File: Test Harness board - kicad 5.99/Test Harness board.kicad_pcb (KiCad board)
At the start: 4 copper layers, 233 x 70 mm, 32 parts, among them U1 TCA9548APWR

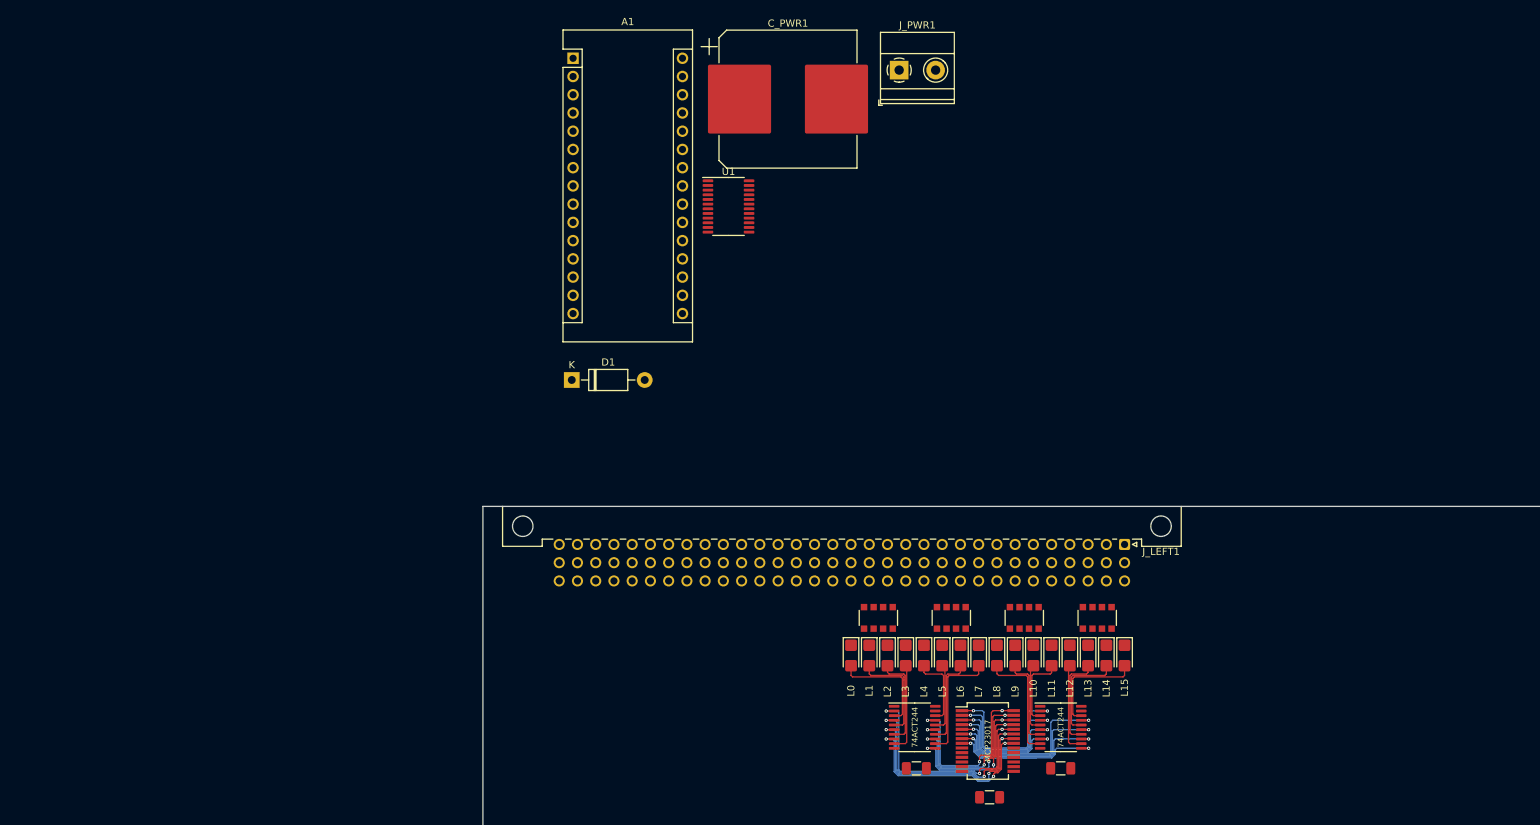
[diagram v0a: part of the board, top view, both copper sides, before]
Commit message: add the components to display the MAR bits
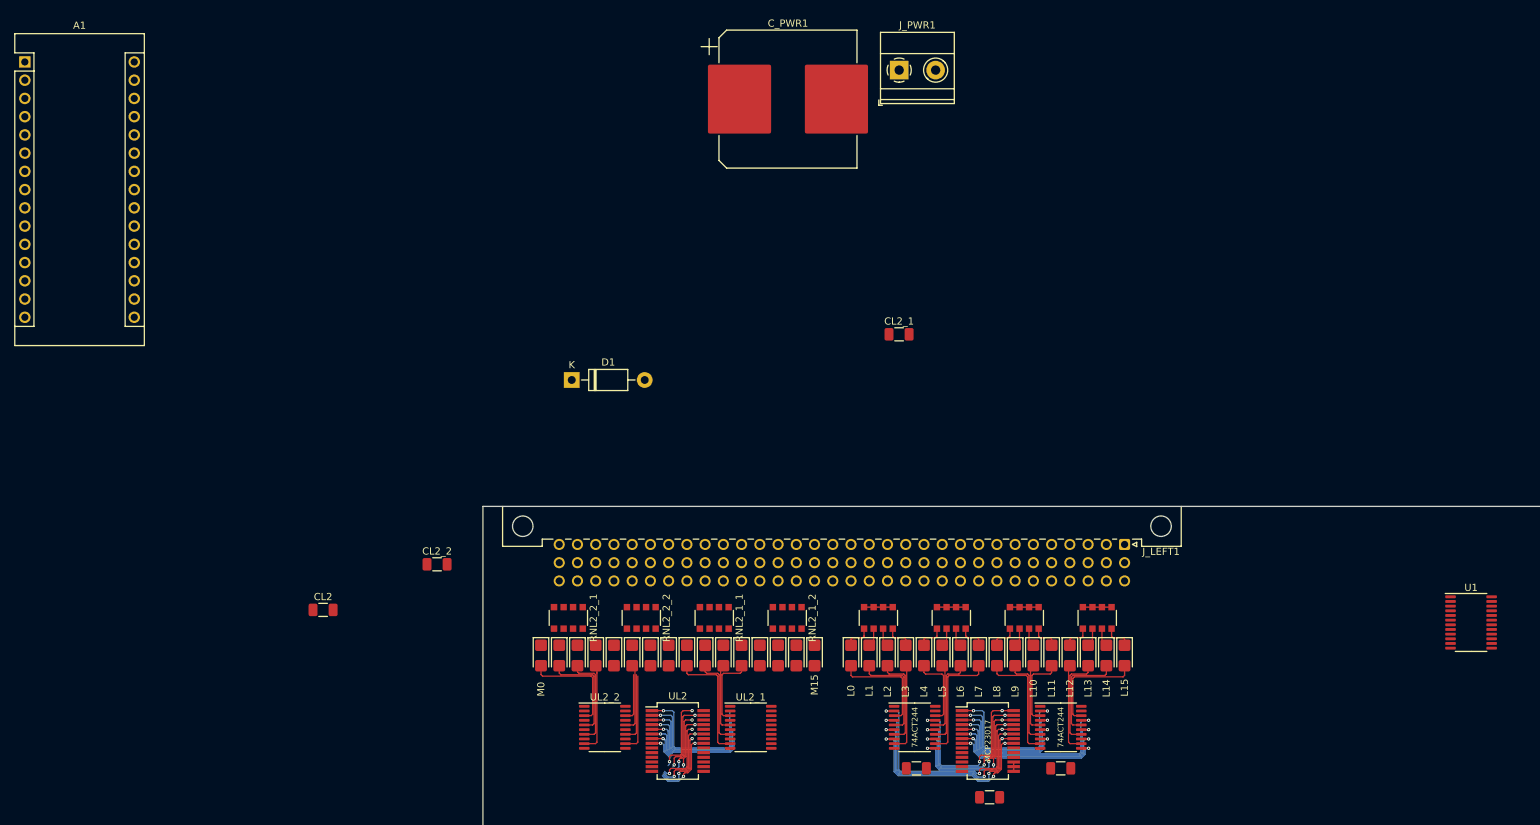
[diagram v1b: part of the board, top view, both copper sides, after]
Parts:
- added CL2: C_Small, Capacitor_SMD:C_1206_3216Metric, F.Cu at (9.74, 84.4)
- added CL2_1: C_Small, Capacitor_SMD:C_1206_3216Metric, F.Cu at (90.0, 46.0)
- added CL2_2: C_Small, Capacitor_SMD:C_1206_3216Metric, F.Cu at (25.6, 78.1)
- added D_MAR0: LED_Small, LED_SMD:LED_1206_3216Metric_Castellated, F.Cu at (40.1, 90.8)
- added D_MAR1: LED_Small, LED_SMD:LED_1206_3216Metric_Castellated, F.Cu at (42.6, 90.8)
- added D_MAR10: LED_Small, LED_SMD:LED_1206_3216Metric_Castellated, F.Cu at (65.5, 90.8)
- added D_MAR11: LED_Small, LED_SMD:LED_1206_3216Metric_Castellated, F.Cu at (68.0, 90.8)
- added D_MAR12: LED_Small, LED_SMD:LED_1206_3216Metric_Castellated, F.Cu at (70.6, 90.8)
- added D_MAR13: LED_Small, LED_SMD:LED_1206_3216Metric_Castellated, F.Cu at (73.1, 90.8)
- added D_MAR14: LED_Small, LED_SMD:LED_1206_3216Metric_Castellated, F.Cu at (75.7, 90.8)
- added D_MAR15: LED_Small, LED_SMD:LED_1206_3216Metric_Castellated, F.Cu at (78.2, 90.8)
- added D_MAR2: LED_Small, LED_SMD:LED_1206_3216Metric_Castellated, F.Cu at (45.2, 90.8)
- added D_MAR3: LED_Small, LED_SMD:LED_1206_3216Metric_Castellated, F.Cu at (47.7, 90.8)
- added D_MAR4: LED_Small, LED_SMD:LED_1206_3216Metric_Castellated, F.Cu at (50.2, 90.8)
- added D_MAR5: LED_Small, LED_SMD:LED_1206_3216Metric_Castellated, F.Cu at (52.8, 90.8)
- added D_MAR6: LED_Small, LED_SMD:LED_1206_3216Metric_Castellated, F.Cu at (55.3, 90.8)
- added D_MAR7: LED_Small, LED_SMD:LED_1206_3216Metric_Castellated, F.Cu at (57.9, 90.8)
- added D_MAR8: LED_Small, LED_SMD:LED_1206_3216Metric_Castellated, F.Cu at (60.4, 90.8)
- added D_MAR9: LED_Small, LED_SMD:LED_1206_3216Metric_Castellated, F.Cu at (63.0, 90.8)
- added RNL2_1_1: R_Pack04, Resistor_SMD:R_Array_Convex_4x1206, F.Cu at (64.2, 85.5)
- added RNL2_1_2: R_Pack04, Resistor_SMD:R_Array_Convex_4x1206, F.Cu at (74.4, 85.5)
- added RNL2_2_1: R_Pack04, Resistor_SMD:R_Array_Convex_4x1206, F.Cu at (43.9, 85.5)
- added RNL2_2_2: R_Pack04, Resistor_SMD:R_Array_Convex_4x1206, F.Cu at (54.1, 85.5)
- added UL2: MCP23017, Package_SO:SSOP-28_5.3x10.2mm_P0.65mm, F.Cu at (59.1, 102.7)
- added UL2_1: 74ACT244, Package_SO:TSSOP-20_4.4x6.5mm_P0.65mm, F.Cu at (69.3, 100.8)
- added UL2_2: 74ACT244, Package_SO:TSSOP-20_4.4x6.5mm_P0.65mm, F.Cu at (49.0, 100.8)
- moved U1 118.5 mm to (169.6, 86.2)
- moved A1 76.4 mm to (-31.8, 8.10)
- renumbered C1 to CL1, C1_1 to CL1_1, C1_2 to CL1_2, RN1_1_1 to RNL1_1_1, RN1_1_2 to RNL1_1_2, RN1_2_1 to RNL1_2_1, RN1_2_2 to RNL1_2_2
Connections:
- J_LEFT1 pad a22: Net-(J_LEFT1-Pada22) -> /Left connector/MAR0
- J_LEFT1 pad a23: Net-(J_LEFT1-Pada23) -> /Left connector/MAR1
- J_LEFT1 pad a24: Net-(J_LEFT1-Pada24) -> /Left connector/MAR2
- J_LEFT1 pad a25: Net-(J_LEFT1-Pada25) -> /Left connector/MAR3
- J_LEFT1 pad a26: Net-(J_LEFT1-Pada26) -> /Left connector/MAR4
- J_LEFT1 pad a27: Net-(J_LEFT1-Pada27) -> /Left connector/MAR5
- J_LEFT1 pad a28: Net-(J_LEFT1-Pada28) -> /Left connector/MAR6
- J_LEFT1 pad a29: Net-(J_LEFT1-Pada29) -> /Left connector/MAR7
- J_LEFT1 pad a30: Net-(J_LEFT1-Pada30) -> /Left connector/MAR8
- J_LEFT1 pad a31: Net-(J_LEFT1-Pada31) -> /Left connector/MAR9
- J_LEFT1 pad b1: (no net) -> Net-(J_LEFT1-Padb1)
- J_LEFT1 pad b10: (no net) -> Net-(J_LEFT1-Padb10)
- J_LEFT1 pad b11: (no net) -> Net-(J_LEFT1-Padb11)
- J_LEFT1 pad b12: (no net) -> Net-(J_LEFT1-Padb12)
- J_LEFT1 pad b13: (no net) -> Net-(J_LEFT1-Padb13)
- J_LEFT1 pad b14: (no net) -> Net-(J_LEFT1-Padb14)
- J_LEFT1 pad b15: (no net) -> Net-(J_LEFT1-Padb15)
- J_LEFT1 pad b16: (no net) -> Net-(J_LEFT1-Padb16)
- J_LEFT1 pad b17: (no net) -> Net-(J_LEFT1-Padb17)
- J_LEFT1 pad b18: (no net) -> Net-(J_LEFT1-Padb18)
- J_LEFT1 pad b19: (no net) -> Net-(J_LEFT1-Padb19)
- J_LEFT1 pad b2: (no net) -> Net-(J_LEFT1-Padb2)
- J_LEFT1 pad b20: (no net) -> Net-(J_LEFT1-Padb20)
- J_LEFT1 pad b21: (no net) -> Net-(J_LEFT1-Padb21)
- J_LEFT1 pad b22: (no net) -> Net-(J_LEFT1-Padb22)
- J_LEFT1 pad b23: (no net) -> Net-(J_LEFT1-Padb23)
- J_LEFT1 pad b24: (no net) -> Net-(J_LEFT1-Padb24)
- J_LEFT1 pad b25: (no net) -> Net-(J_LEFT1-Padb25)
- J_LEFT1 pad b26: (no net) -> Net-(J_LEFT1-Padb26)
- J_LEFT1 pad b27: (no net) -> Net-(J_LEFT1-Padb27)
- J_LEFT1 pad b28: (no net) -> Net-(J_LEFT1-Padb28)
- J_LEFT1 pad b29: (no net) -> Net-(J_LEFT1-Padb29)
- J_LEFT1 pad b3: (no net) -> /Left connector/MAR10
- J_LEFT1 pad b30: (no net) -> Net-(J_LEFT1-Padb30)
- J_LEFT1 pad b31: (no net) -> Net-(J_LEFT1-Padb31)
- J_LEFT1 pad b32: (no net) -> Net-(J_LEFT1-Padb32)
- J_LEFT1 pad b4: (no net) -> /Left connector/MAR11
- J_LEFT1 pad b5: (no net) -> /Left connector/MAR12
- J_LEFT1 pad b6: (no net) -> Net-(J_LEFT1-Padb6)
- J_LEFT1 pad b7: (no net) -> /Left connector/MAR13
- J_LEFT1 pad b8: (no net) -> /Left connector/MAR14
- J_LEFT1 pad b9: (no net) -> /Left connector/MAR15
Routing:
- net /Left connector/MAR15: track 0.00 -> 20.6 mm, vias 0 -> 1
- net /Left connector/MAR14: track 0.00 -> 19.2 mm, vias 0 -> 1
- net /Left connector/MAR13: track 0.00 -> 17.7 mm, vias 0 -> 1
- net GND: track 0.00 -> 17.3 mm
- net /Left connector/D_MAR8: track 0.00 -> 16.5 mm
- net /Left connector/MAR12: track 0.00 -> 16.2 mm, vias 0 -> 1
- net /Left connector/D_MAR0: track 0.00 -> 14.9 mm
- net /Left connector/D_MAR1: track 0.00 -> 14.1 mm
- net /Left connector/D_MAR2: track 0.00 -> 13.3 mm
- net /Left connector/D_MAR9: track 0.00 -> 12.7 mm
- net /Left connector/D_MAR3: track 0.00 -> 12.6 mm
- net /Left connector/D_MAR7: track 0.00 -> 11.0 mm
- net /Left connector/MAR0: track 0.00 -> 10.6 mm, vias 0 -> 2
- net /Left connector/D_MAR11: track 0.00 -> 10.5 mm
- net /Left connector/L5: track 31.6 -> 41.7 mm, vias 3 -> 5
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
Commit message: restart on the test harness, made a more compact design (will need the 4 layers though)
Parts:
- added CL3: C_Small, Capacitor_SMD:C_1206_3216Metric, F.Cu at (183.3, 145.9)
- added CL3_1: C_Small, Capacitor_SMD:C_1206_3216Metric, F.Cu at (183.9, 165.8)
- added CL3_2: C_Small, Capacitor_SMD:C_1206_3216Metric, F.Cu at (193.7, 167.4)
- added CL4: C_Small, Capacitor_SMD:C_1206_3216Metric, F.Cu at (191.3, 152.6)
- added CL4_1: C_Small, Capacitor_SMD:C_1206_3216Metric, F.Cu at (191.2, 159.2)
- added CL4_2: C_Small, Capacitor_SMD:C_1206_3216Metric, F.Cu at (64.3, 142.6)
- added CL5: C_Small, Capacitor_SMD:C_1206_3216Metric, F.Cu at (73.4, 140.9)
- added CL5_1: C_Small, Capacitor_SMD:C_1206_3216Metric, F.Cu at (64.9, 144.3)
- added CL5_2: C_Small, Capacitor_SMD:C_1206_3216Metric, F.Cu at (58.0, 142.8)
- added D_A0: LED_Small, LED_SMD:LED_1206_3216Metric_Castellated, F.Cu at (66.7, 106.8)
- added D_A1: LED_Small, LED_SMD:LED_1206_3216Metric_Castellated, F.Cu at (69.2, 106.8)
- added D_A10: LED_Small, LED_SMD:LED_1206_3216Metric_Castellated, F.Cu at (93.9, 106.8)
- added D_A11: LED_Small, LED_SMD:LED_1206_3216Metric_Castellated, F.Cu at (96.4, 106.8)
- added D_A12: LED_Small, LED_SMD:LED_1206_3216Metric_Castellated, F.Cu at (98.9, 106.8)
- added D_A13: LED_Small, LED_SMD:LED_1206_3216Metric_Castellated, F.Cu at (101.4, 106.8)
- added D_A14: LED_Small, LED_SMD:LED_1206_3216Metric_Castellated, F.Cu at (104.7, 106.8)
- added D_A15: LED_Small, LED_SMD:LED_1206_3216Metric_Castellated, F.Cu at (107.2, 106.8)
- added D_A16: LED_Small, LED_SMD:LED_1206_3216Metric_Castellated, F.Cu at (109.7, 106.8)
- added D_A17: LED_Small, LED_SMD:LED_1206_3216Metric_Castellated, F.Cu at (112.2, 106.8)
- added D_A18: LED_Small, LED_SMD:LED_1206_3216Metric_Castellated, F.Cu at (115.4, 106.8)
- added D_A19: LED_Small, LED_SMD:LED_1206_3216Metric_Castellated, F.Cu at (117.9, 106.8)
- added D_A2: LED_Small, LED_SMD:LED_1206_3216Metric_Castellated, F.Cu at (72.4, 106.8)
- added D_A20: LED_Small, LED_SMD:LED_1206_3216Metric_Castellated, F.Cu at (120.4, 106.8)
- added D_A21: LED_Small, LED_SMD:LED_1206_3216Metric_Castellated, F.Cu at (122.9, 106.8)
- added D_A3: LED_Small, LED_SMD:LED_1206_3216Metric_Castellated, F.Cu at (74.9, 106.8)
- added D_A4: LED_Small, LED_SMD:LED_1206_3216Metric_Castellated, F.Cu at (77.4, 106.8)
- added D_A5: LED_Small, LED_SMD:LED_1206_3216Metric_Castellated, F.Cu at (79.9, 106.8)
- added D_A6: LED_Small, LED_SMD:LED_1206_3216Metric_Castellated, F.Cu at (83.2, 106.8)
- added D_A7: LED_Small, LED_SMD:LED_1206_3216Metric_Castellated, F.Cu at (85.7, 106.8)
- added D_A8: LED_Small, LED_SMD:LED_1206_3216Metric_Castellated, F.Cu at (88.2, 106.8)
- added D_A9: LED_Small, LED_SMD:LED_1206_3216Metric_Castellated, F.Cu at (90.7, 106.8)
- added D_D0: LED_Small, LED_SMD:LED_1206_3216Metric_Castellated, F.Cu at (38.4, 106.8)
- added D_D1: LED_Small, LED_SMD:LED_1206_3216Metric_Castellated, F.Cu at (40.9, 106.8)
- added D_D2: LED_Small, LED_SMD:LED_1206_3216Metric_Castellated, F.Cu at (43.4, 106.8)
- added D_D3: LED_Small, LED_SMD:LED_1206_3216Metric_Castellated, F.Cu at (45.9, 106.8)
- added D_D4: LED_Small, LED_SMD:LED_1206_3216Metric_Castellated, F.Cu at (49.2, 106.8)
- added D_D5: LED_Small, LED_SMD:LED_1206_3216Metric_Castellated, F.Cu at (51.7, 106.8)
- added D_D6: LED_Small, LED_SMD:LED_1206_3216Metric_Castellated, F.Cu at (54.2, 106.8)
- added D_D7: LED_Small, LED_SMD:LED_1206_3216Metric_Castellated, F.Cu at (56.7, 106.8)
- added D_IR2: LED_Small, LED_SMD:LED_1206_3216Metric_Castellated, F.Cu at (40.9, 121.8)
- added D_IR3: LED_Small, LED_SMD:LED_1206_3216Metric_Castellated, F.Cu at (43.4, 121.8)
- added D_MEMORY1: LED_Small, LED_SMD:LED_1206_3216Metric_Castellated, F.Cu at (63.9, 121.8)
- added D_MEMREF1: LED_Small, LED_SMD:LED_1206_3216Metric_Castellated, F.Cu at (61.4, 121.8)
- added D_TEST1: LED_Small, LED_SMD:LED_1206_3216Metric_Castellated, F.Cu at (179.6, 151.4)
- added D_TEST2: LED_Small, LED_SMD:LED_1206_3216Metric_Castellated, F.Cu at (202.1, 145.1)
- added D_XL_MDR_HI1: LED_Small, LED_SMD:LED_1206_3216Metric_Castellated, F.Cu at (46.7, 121.8)
- added D_XL_MDR_LO1: LED_Small, LED_SMD:LED_1206_3216Metric_Castellated, F.Cu at (49.2, 121.8)
- added D__IR1: LED_Small, LED_SMD:LED_1206_3216Metric_Castellated, F.Cu at (38.4, 121.8)
- added D__IRQ4: LED_Small, LED_SMD:LED_1206_3216Metric_Castellated, F.Cu at (77.9, 121.8)
- added D__PSEL1: LED_Small, LED_SMD:LED_1206_3216Metric_Castellated, F.Cu at (58.2, 121.8)
- added D__RD1: LED_Small, LED_SMD:LED_1206_3216Metric_Castellated, F.Cu at (54.9, 121.8)
- added D__RESET1: LED_Small, LED_SMD:LED_1206_3216Metric_Castellated, F.Cu at (67.2, 121.8)
- added D__STOP_CLK1: LED_Small, LED_SMD:LED_1206_3216Metric_Castellated, F.Cu at (69.7, 121.8)
- added D__WR1: LED_Small, LED_SMD:LED_1206_3216Metric_Castellated, F.Cu at (52.4, 121.8)
- added RNL3_1_1: R_Pack04, Resistor_SMD:R_Array_Convex_4x1206, F.Cu at (106.4, 101.5)
- added RNL3_1_2: R_Pack04, Resistor_SMD:R_Array_Convex_4x1206, F.Cu at (121.4, 101.5)
- added RNL3_2_1: R_Pack04, Resistor_SMD:R_Array_Convex_4x1206, F.Cu at (85.2, 101.5)
- added RNL3_2_2: R_Pack04, Resistor_SMD:R_Array_Convex_4x1206, F.Cu at (99.7, 101.5)
- added RNL4_1_1: R_Pack04, Resistor_SMD:R_Array_Convex_4x1206, F.Cu at (63.2, 101.5)
- added RNL4_1_2: R_Pack04, Resistor_SMD:R_Array_Convex_4x1206, F.Cu at (78.2, 101.5)
- added RNL4_2_1: R_Pack04, Resistor_SMD:R_Array_Convex_4x1206, F.Cu at (40.2, 101.6)
- added RNL4_2_2: R_Pack04, Resistor_SMD:R_Array_Convex_4x1206, F.Cu at (54.9, 101.6)
- added RNL5_1_1: R_Pack04, Resistor_SMD:R_Array_Convex_4x1206, F.Cu at (63.2, 116.6)
- added RNL5_1_2: R_Pack04, Resistor_SMD:R_Array_Convex_4x1206, F.Cu at (78.7, 116.6)
- added RNL5_2_1: R_Pack04, Resistor_SMD:R_Array_Convex_4x1206, F.Cu at (56.4, 116.6)
- added RNL5_2_2: R_Pack04, Resistor_SMD:R_Array_Convex_4x1206, F.Cu at (40.2, 116.6)
- added UL3: MCP23017, Package_SO:SSOP-28_5.3x10.2mm_P0.65mm, F.Cu at (107.9, 132.3)
- added UL3_1: 74ACT244, Package_SO:TSSOP-20_4.4x6.5mm_P0.65mm, F.Cu at (115.6, 116.7)
- added UL3_2: 74ACT244, Package_SO:TSSOP-20_4.4x6.5mm_P0.65mm, F.Cu at (105.9, 116.7)
- added UL4: MCP23017, Package_SO:SSOP-28_5.3x10.2mm_P0.65mm, F.Cu at (95.3, 118.8)
- added UL4_1: 74ACT244, Package_SO:TSSOP-20_4.4x6.5mm_P0.65mm, F.Cu at (71.1, 115.2)
- added UL4_2: 74ACT244, Package_SO:TSSOP-20_4.4x6.5mm_P0.65mm, F.Cu at (48.2, 115.3)
- added UL5: MCP23017, Package_SO:SSOP-28_5.3x10.2mm_P0.65mm, F.Cu at (95.4, 132.3)
- added UL5_1: 74ACT244, Package_SO:TSSOP-20_4.4x6.5mm_P0.65mm, F.Cu at (54.2, 133.8)
- added UL5_2: 74ACT244, Package_SO:TSSOP-20_4.4x6.5mm_P0.65mm, F.Cu at (40.9, 133.8)
- C_PWR1: footprint Capacitor_SMD:CP_Elec_18x22 -> Capacitor_SMD:CP_Elec_8x10
- D1: value 1N4001 -> 1N4007FLTR; footprint Diode_THT:D_DO-41_SOD81_P10.16mm_Horizontal -> Diode_SMD:D_SOD-123F
- moved A1 194.6 mm to (140.9, 97.8)
- moved J_PWR1 131.5 mm to (129.0, 134.8)
- moved C_PWR1 117.7 mm to (132.2, 115.8)
- moved D1 111.7 mm to (129.0, 125.3), turned to -90 degrees
- moved CL1 94.8 mm to (197.3, 115.0)
- moved CL1_1 94.8 mm to (207.2, 111.0)
- moved CL1_2 94.8 mm to (187.1, 111.0)
- moved UL2 73.1 mm to (132.2, 103.8)
- moved U1 37.2 mm to (148.5, 116.8)
- moved UL1 32.3 mm to (132.2, 90.3)
- moved D_MAR3 2.06 mm to (45.9, 91.8)
- moved D_L12 2.05 mm to (115.5, 91.8)
- moved D_MAR2 2.02 mm to (43.4, 91.8)
- moved D_L13 2.02 mm to (118.0, 91.8)
- moved RNL2_2_1 2.00 mm to (42.2, 86.6)
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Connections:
- J_LEFT1 pad b10: Net-(J_LEFT1-Padb10) -> /Left connector/MEMREF
- J_LEFT1 pad b14: Net-(J_LEFT1-Padb14) -> /Left connector/_RESET
- J_LEFT1 pad b15: Net-(J_LEFT1-Padb15) -> /Left connector/_STOP_CLK
- J_LEFT1 pad b16: Net-(J_LEFT1-Padb16) -> /Left connector/_WR
- J_LEFT1 pad b18: Net-(J_LEFT1-Padb18) -> /Left connector/XL_MDR_HI
- J_LEFT1 pad b19: Net-(J_LEFT1-Padb19) -> /Left connector/XL_MDR_LO
- J_LEFT1 pad b2: Net-(J_LEFT1-Padb2) -> /Left connector/MEMORY
- J_LEFT1 pad b25: Net-(J_LEFT1-Padb25) -> /Left connector/_RD
- J_LEFT1 pad b26: Net-(J_LEFT1-Padb26) -> /Left connector/_IRQ4
- J_LEFT1 pad b28: Net-(J_LEFT1-Padb28) -> /Left connector/IR1
- J_LEFT1 pad b29: Net-(J_LEFT1-Padb29) -> /Left connector/IR2
- J_LEFT1 pad b30: Net-(J_LEFT1-Padb30) -> /Left connector/IR3
- J_LEFT1 pad b6: Net-(J_LEFT1-Padb6) -> /Left connector/_PSEL1
- J_LEFT1 pad c1: (no net) -> /Left connector/A0
- J_LEFT1 pad c10: (no net) -> /Left connector/A8
- J_LEFT1 pad c11: (no net) -> /Left connector/A9
- J_LEFT1 pad c12: (no net) -> /Left connector/A10
- J_LEFT1 pad c13: (no net) -> /Left connector/A11
- J_LEFT1 pad c14: (no net) -> /Left connector/A12
- J_LEFT1 pad c15: (no net) -> /Left connector/A13
- J_LEFT1 pad c16: (no net) -> /Left connector/A14
- J_LEFT1 pad c17: (no net) -> /Left connector/A15
- J_LEFT1 pad c18: (no net) -> /Left connector/A16
- J_LEFT1 pad c19: (no net) -> /Left connector/A17
- J_LEFT1 pad c2: (no net) -> /Left connector/A1
- J_LEFT1 pad c20: (no net) -> /Left connector/A18
- J_LEFT1 pad c21: (no net) -> /Left connector/A19
- J_LEFT1 pad c22: (no net) -> /Left connector/A20
- J_LEFT1 pad c23: (no net) -> /Left connector/A21
- J_LEFT1 pad c24: (no net) -> /Left connector/D0
- J_LEFT1 pad c25: (no net) -> /Left connector/D1
- J_LEFT1 pad c26: (no net) -> /Left connector/D2
- J_LEFT1 pad c27: (no net) -> /Left connector/D3
- J_LEFT1 pad c28: (no net) -> /Left connector/D4
- J_LEFT1 pad c29: (no net) -> /Left connector/D5
- J_LEFT1 pad c3: (no net) -> /Left connector/A2
- J_LEFT1 pad c30: (no net) -> /Left connector/D6
- J_LEFT1 pad c31: (no net) -> /Left connector/D7
- J_LEFT1 pad c32: (no net) -> Net-(J_LEFT1-Padc32)
- J_LEFT1 pad c4: (no net) -> /Left connector/A3
- J_LEFT1 pad c5: (no net) -> /Left connector/A4
- J_LEFT1 pad c6: (no net) -> /Left connector/A5
- J_LEFT1 pad c7: (no net) -> /Left connector/A6
- J_LEFT1 pad c8: (no net) -> /Left connector/A7
- J_LEFT1 pad c9: (no net) -> Net-(J_LEFT1-Padc9)
- UL2 pad 15: GND -> +5V
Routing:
- net /Left connector/D5: track 0.00 -> 64.3 mm, vias 0 -> 2
- net /Left connector/D4: track 0.00 -> 63.5 mm, vias 0 -> 2
- net /Left connector/D7: track 0.00 -> 61.5 mm, vias 0 -> 2
- net /Left connector/D6: track 0.00 -> 60.3 mm, vias 0 -> 2
- net /Left connector/D1: track 0.00 -> 56.0 mm, vias 0 -> 2
- net /Left connector/D0: track 0.00 -> 55.0 mm, vias 0 -> 2
- net /Left connector/D3: track 0.00 -> 52.7 mm, vias 0 -> 2
- net /Left connector/D2: track 0.00 -> 51.9 mm, vias 0 -> 2
- net /Left connector/L4: track 42.7 -> 0.00 mm, vias 5 -> 0
- net /Left connector/L5: track 41.7 -> 0.00 mm, vias 5 -> 0
- net /Left connector/L6: track 39.7 -> 0.00 mm, vias 5 -> 0
- net /Left connector/L7: track 37.4 -> 0.00 mm, vias 5 -> 0
- net /Left connector/L1: track 34.5 -> 0.00 mm, vias 5 -> 0
- net /Left connector/L2: track 31.2 -> 0.00 mm, vias 5 -> 0
- net /Left connector/D_A6: track 0.00 -> 30.3 mm
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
